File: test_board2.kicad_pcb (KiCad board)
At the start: 2 copper layers, 73.7 x 101.6 mm, 67 parts, among them U1 SM220, U2 AS1116

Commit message: After 1st design review
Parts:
- added BT1, BT2: 1.5V, Synapse:BATT_2466, F.Cu at (177.8, 152.3)
- added C1, C18, C2: 100nF, Capacitors_SMD:C_0603, F.Cu at (177.8, 152.3)
- added C10, C12, C14, C8: 0.1uF, Capacitors_SMD:C_0603, F.Cu at (177.8, 152.3)
- added C11, C13, C15, C17, C19, C7, C9: 4.7uF, Capacitors_SMD:C_0603, F.Cu at (177.8, 152.3)
- added C16, C3: 10uF, Capacitors_SMD:C_0603, F.Cu at (177.8, 152.3)
- added C4: 10nF, Capacitors_SMD:C_0603, F.Cu at (177.8, 152.3)
- added C5, C6: 47pF, Capacitors_SMD:C_0603, F.Cu at (177.8, 152.3)
- added D65: LED, w_smd_leds:Led_0603, F.Cu at (172.2, 150.7)
- added D66, D67, D68: LED, w_smd_leds:Led_0603, F.Cu at (177.8, 152.3)
- added D69, D70, D71, D72, D73, D74, D75: 1N4148W, Diodes_SMD:SOD-123, F.Cu at (177.8, 152.3)
- added FB1: 600 OHM 500MA, Resistors_SMD:R_0603, F.Cu at (177.8, 152.3)
- added L1: 4.7uH 0.9A, Synapse:TYS-2, F.Cu at (177.8, 152.3)
- added P1: USB_B, w_conn_pc:conn_usb_B_micro_smd-2, F.Cu at (152.7, 152.7)
- added P2, P3: CONN_01X08, Pin_Headers:Pin_Header_Straight_1x08, F.Cu at (177.8, 152.3)
- added P4: CONN_01X10, Pin_Headers:Pin_Header_Straight_1x10, F.Cu at (177.8, 152.3)
- added P5: CONN_01X06, Pin_Headers:Pin_Header_Straight_1x06, F.Cu at (177.8, 152.3)
- added P6: CONN_02X03, Pin_Headers:Pin_Header_Straight_2x03, F.Cu at (177.8, 152.3)
- added Q1: ZXMN2F30FHCT-ND, TO_SOT_Packages_SMD:SOT-23, F.Cu at (164.7, 149.9)
- added R10: 100k, Resistors_SMD:R_0603, F.Cu at (177.8, 152.3)
- added R11: 1M, Resistors_SMD:R_0603, F.Cu at (177.8, 152.3)
- added R2, R3: 27, Resistors_SMD:R_0603, F.Cu at (177.8, 152.3)
- added R4, R5, R6: 270, Resistors_SMD:R_0603, F.Cu at (177.8, 152.3)
- added R7, R8: 1k, Resistors_SMD:R_0603, F.Cu at (177.8, 152.3)
- added R9: 200k, Resistors_SMD:R_0603, F.Cu at (177.8, 152.3)
- added SW1: SWITCH_DPDT, Synapse:SO-DPDT-6, F.Cu at (177.8, 152.3)
- added SW2, SW3, SW4: SW_PUSH, Buttons_Switches_SMD:SW_SPST_PTS645, F.Cu at (177.8, 152.3)
- added SW5: SW_DIP_8, Synapse:DIPSW-16, F.Cu at (177.8, 152.3)
- added U3: FT230XS, Housings_SSOP:SSOP-16_3.9x4.9mm_Pitch0.635mm, F.Cu at (138.3, 151.5)
- added U4: LD1117S33CTR, TO_SOT_Packages_SMD:SOT-223, F.Cu at (198.4, 152.1)
- added U5: LIS3DH, Synapse:LGA16_3x3, F.Cu at (177.8, 152.3)
- added U6: TPS61070, TO_SOT_Packages_SMD:TSOT-6-MK06A, F.Cu at (177.8, 152.3)
- D2: value LED -> 1N4148W
- U2: value AS1116 -> AS1115
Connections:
- D1 pad 1: Net-(D1-Pad1) -> /STATUS_LED
- D1 pad 2: /SEGA -> Net-(D1-Pad2)
- D10 pad 1: Net-(D10-Pad1) -> /LED_matrix/DIG7
- D10 pad 2: /SEGB -> /LED_matrix/SEGA
- D11 pad 1: Net-(D11-Pad1) -> /LED_matrix/DIG0
- D11 pad 2: /SEGB -> /LED_matrix/SEGB
- D12 pad 1: Net-(D12-Pad1) -> /LED_matrix/DIG1
- D12 pad 2: /SEGB -> /LED_matrix/SEGB
- D13 pad 1: Net-(D13-Pad1) -> /LED_matrix/DIG2
- D13 pad 2: /SEGB -> /LED_matrix/SEGB
- D14 pad 1: Net-(D14-Pad1) -> /LED_matrix/DIG3
- D14 pad 2: /SEGB -> /LED_matrix/SEGB
- D15 pad 1: Net-(D15-Pad1) -> /LED_matrix/DIG4
- D15 pad 2: /SEGB -> /LED_matrix/SEGB
- D16 pad 1: Net-(D16-Pad1) -> /LED_matrix/DIG5
- D16 pad 2: /SEGB -> /LED_matrix/SEGB
- D17 pad 1: Net-(D1-Pad1) -> /LED_matrix/DIG6
- D17 pad 2: /SEGC -> /LED_matrix/SEGB
- D18 pad 1: Net-(D10-Pad1) -> /LED_matrix/DIG7
- D18 pad 2: /SEGC -> /LED_matrix/SEGB
- D19 pad 1: Net-(D11-Pad1) -> /LED_matrix/DIG0
- D19 pad 2: /SEGC -> /LED_matrix/SEGC
- D2 pad 1: Net-(D10-Pad1) -> Net-(D2-Pad1)
- D2 pad 2: /SEGA -> /LED_matrix/SEGA
- D20 pad 1: Net-(D12-Pad1) -> /LED_matrix/DIG1
- D20 pad 2: /SEGC -> /LED_matrix/SEGC
- D21 pad 1: Net-(D13-Pad1) -> /LED_matrix/DIG2
- D21 pad 2: /SEGC -> /LED_matrix/SEGC
- D22 pad 1: Net-(D14-Pad1) -> /LED_matrix/DIG3
- D22 pad 2: /SEGC -> /LED_matrix/SEGC
- D23 pad 1: Net-(D15-Pad1) -> /LED_matrix/DIG4
- D23 pad 2: /SEGC -> /LED_matrix/SEGC
- D24 pad 1: Net-(D16-Pad1) -> /LED_matrix/DIG5
- D24 pad 2: /SEGC -> /LED_matrix/SEGC
- D25 pad 1: Net-(D1-Pad1) -> /LED_matrix/DIG6
- D25 pad 2: /SEGD -> /LED_matrix/SEGC
- D26 pad 1: Net-(D10-Pad1) -> /LED_matrix/DIG7
- D26 pad 2: /SEGD -> /LED_matrix/SEGC
- D27 pad 1: Net-(D11-Pad1) -> /LED_matrix/DIG0
- D27 pad 2: /SEGD -> /LED_matrix/SEGD
- D28 pad 1: Net-(D12-Pad1) -> /LED_matrix/DIG1
- D28 pad 2: /SEGD -> /LED_matrix/SEGD
- D29 pad 1: Net-(D13-Pad1) -> /LED_matrix/DIG2
- D29 pad 2: /SEGD -> /LED_matrix/SEGD
- D3 pad 1: Net-(D11-Pad1) -> /LED_matrix/DIG0
- D3 pad 2: /SEGA -> /LED_matrix/SEGA
- D30 pad 1: Net-(D14-Pad1) -> /LED_matrix/DIG3
- D30 pad 2: /SEGD -> /LED_matrix/SEGD
- D31 pad 1: Net-(D15-Pad1) -> /LED_matrix/DIG4
- D31 pad 2: /SEGD -> /LED_matrix/SEGD
- D32 pad 1: Net-(D16-Pad1) -> /LED_matrix/DIG5
- D32 pad 2: /SEGD -> /LED_matrix/SEGD
- D33 pad 1: Net-(D1-Pad1) -> /LED_matrix/DIG6
- D33 pad 2: /SEGE -> /LED_matrix/SEGD
- D34 pad 1: Net-(D10-Pad1) -> /LED_matrix/DIG7
- D34 pad 2: /SEGE -> /LED_matrix/SEGD
- D35 pad 1: Net-(D11-Pad1) -> /LED_matrix/DIG0
- D35 pad 2: /SEGE -> /LED_matrix/SEGE
- D36 pad 1: Net-(D12-Pad1) -> /LED_matrix/DIG1
- D36 pad 2: /SEGE -> /LED_matrix/SEGE
- D37 pad 1: Net-(D13-Pad1) -> /LED_matrix/DIG2
- D37 pad 2: /SEGE -> /LED_matrix/SEGE
- D38 pad 1: Net-(D14-Pad1) -> /LED_matrix/DIG3
- D38 pad 2: /SEGE -> /LED_matrix/SEGE
- D39 pad 1: Net-(D15-Pad1) -> /LED_matrix/DIG4
- D39 pad 2: /SEGE -> /LED_matrix/SEGE
- D4 pad 1: Net-(D12-Pad1) -> /LED_matrix/DIG1
- D4 pad 2: /SEGA -> /LED_matrix/SEGA
- D40 pad 1: Net-(D16-Pad1) -> /LED_matrix/DIG5
- D40 pad 2: /SEGE -> /LED_matrix/SEGE
- D41 pad 1: Net-(D1-Pad1) -> /LED_matrix/DIG6
- D41 pad 2: /SEGF -> /LED_matrix/SEGE
- D42 pad 1: Net-(D10-Pad1) -> /LED_matrix/DIG7
- D42 pad 2: /SEGF -> /LED_matrix/SEGE
- D43 pad 1: Net-(D11-Pad1) -> /LED_matrix/DIG0
- D43 pad 2: /SEGF -> /LED_matrix/SEGF
- D44 pad 1: Net-(D12-Pad1) -> /LED_matrix/DIG1
- D44 pad 2: /SEGF -> /LED_matrix/SEGF
- D45 pad 1: Net-(D13-Pad1) -> /LED_matrix/DIG2
- D45 pad 2: /SEGF -> /LED_matrix/SEGF
- D46 pad 1: Net-(D14-Pad1) -> /LED_matrix/DIG3
- D46 pad 2: /SEGF -> /LED_matrix/SEGF
- D47 pad 1: Net-(D15-Pad1) -> /LED_matrix/DIG4
- D47 pad 2: /SEGF -> /LED_matrix/SEGF
- D48 pad 1: Net-(D16-Pad1) -> /LED_matrix/DIG5
- D48 pad 2: /SEGF -> /LED_matrix/SEGF
- D49 pad 1: Net-(D1-Pad1) -> /LED_matrix/DIG6
- D49 pad 2: /SEGG -> /LED_matrix/SEGF
- D5 pad 1: Net-(D13-Pad1) -> /LED_matrix/DIG2
- D5 pad 2: /SEGA -> /LED_matrix/SEGA
- D50 pad 1: Net-(D10-Pad1) -> /LED_matrix/DIG7
- D50 pad 2: /SEGG -> /LED_matrix/SEGF
- D51 pad 1: Net-(D11-Pad1) -> /LED_matrix/DIG0
- D51 pad 2: /SEGG -> /LED_matrix/SEGG
- D52 pad 1: Net-(D12-Pad1) -> /LED_matrix/DIG1
- D52 pad 2: /SEGG -> /LED_matrix/SEGG
- D53 pad 1: Net-(D13-Pad1) -> /LED_matrix/DIG2
- D53 pad 2: /SEGG -> /LED_matrix/SEGG
- D54 pad 1: Net-(D14-Pad1) -> /LED_matrix/DIG3
- D54 pad 2: /SEGG -> /LED_matrix/SEGG
- D55 pad 1: Net-(D15-Pad1) -> /LED_matrix/DIG4
- D55 pad 2: /SEGG -> /LED_matrix/SEGG
- D56 pad 1: Net-(D16-Pad1) -> /LED_matrix/DIG5
- D56 pad 2: /SEGG -> /LED_matrix/SEGG
- D57 pad 1: Net-(D1-Pad1) -> /LED_matrix/DIG6
- D57 pad 2: /SEGDP -> /LED_matrix/SEGG
- D58 pad 1: Net-(D10-Pad1) -> /LED_matrix/DIG7
- D58 pad 2: /SEGDP -> /LED_matrix/SEGG
- D59 pad 1: Net-(D11-Pad1) -> /LED_matrix/DIG0
- D59 pad 2: /SEGDP -> /LED_matrix/SEGDP
- D6 pad 1: Net-(D14-Pad1) -> /LED_matrix/DIG3
- D6 pad 2: /SEGA -> /LED_matrix/SEGA
- D60 pad 1: Net-(D12-Pad1) -> /LED_matrix/DIG1
- D60 pad 2: /SEGDP -> /LED_matrix/SEGDP
- D61 pad 1: Net-(D13-Pad1) -> /LED_matrix/DIG2
- D61 pad 2: /SEGDP -> /LED_matrix/SEGDP
- D62 pad 1: Net-(D14-Pad1) -> /LED_matrix/DIG3
- D62 pad 2: /SEGDP -> /LED_matrix/SEGDP
- D63 pad 1: Net-(D15-Pad1) -> /LED_matrix/DIG4
- D63 pad 2: /SEGDP -> /LED_matrix/SEGDP
- D64 pad 1: Net-(D16-Pad1) -> /LED_matrix/DIG5
- D64 pad 2: /SEGDP -> /LED_matrix/SEGDP
- D7 pad 1: Net-(D15-Pad1) -> /LED_matrix/DIG4
- D7 pad 2: /SEGA -> /LED_matrix/SEGA
- D8 pad 1: Net-(D16-Pad1) -> /LED_matrix/DIG5
- D8 pad 2: /SEGA -> /LED_matrix/SEGA
- D9 pad 1: Net-(D1-Pad1) -> /LED_matrix/DIG6
- D9 pad 2: /SEGB -> /LED_matrix/SEGA
- R1 pad 1: VCC -> /LED_matrix/LED_3V
- U1 pad A4: Net-(U1-PadA4) -> /PF0
- U1 pad A5: /SCLK -> Net-(U1-PadA5)
- U1 pad A6: Net-(U1-PadA6) -> /PF4
- U1 pad A7: Net-(U1-PadA7) -> /PF6
- U1 pad B1: /MISO -> Net-(U1-PadB1)
- U1 pad B2: /LED_LD -> /PE3
- U1 pad B3: Net-(U1-PadB3) -> /PE5
- U1 pad B4: /MOSI -> /PF1
- U1 pad B6: Net-(U1-PadB6) -> /PF5
- U1 pad B7: Net-(U1-PadB7) -> /PF7
- U1 pad C1: Net-(U1-PadC1) -> /PE0
- U1 pad C2: Net-(U1-PadC2) -> /PE1
- U1 pad C3: Net-(U1-PadC3) -> /PE4
- U1 pad C4: Net-(U1-PadC4) -> /BTN_RT
- U1 pad C5: Net-(U1-PadC5) -> /PE7
- U1 pad D1: Net-(U1-PadD1) -> /PB5
- U1 pad D2: Net-(U1-PadD2) -> /PB6
- U1 pad D3: Net-(U1-PadD3) -> /PB7
- U1 pad E1: Net-(U1-PadE1) -> /MOSI
- U1 pad E2: Net-(U1-PadE2) -> /MISO
- U1 pad E3: Net-(U1-PadE3) -> /ACC_INT1
- U1 pad F1: Net-(U1-PadF1) -> /BTN_LFT
- U1 pad F2: Net-(U1-PadF2) -> /SCLK
- U1 pad F3: Net-(U1-PadF3) -> I2C_SDA
- U1 pad F4: Net-(U1-PadF4) -> I2C_SCL
- U1 pad G2: Net-(U1-PadG2) -> /*IS_USB
- U1 pad G3: Net-(U1-PadG3) -> /PD4
- U1 pad G4: Net-(U1-PadG4) -> /USB_TXD
- U1 pad G5: Net-(U1-PadG5) -> /STATUS_LED
- U1 pad H2: Net-(U1-PadH2) -> /ACC_INT2
- U1 pad H3: Net-(U1-PadH3) -> LED_PWR_EN
- U1 pad H4: Net-(U1-PadH4) -> /USB_RXD
- U1 pad H5: Net-(U1-PadH5) -> /*RESET
- U2 pad 1: /MOSI -> I2C_SDA
- U2 pad 10: /DIG7 -> /LED_matrix/DIG7
- U2 pad 11: /LED_LD -> Net-(U2-Pad11)
- U2 pad 14: /SCLK -> I2C_SCL
- U2 pad 15: /SEGA -> /LED_matrix/SEGA
- U2 pad 16: /SEGF -> /LED_matrix/SEGF
- U2 pad 17: /SEGB -> /LED_matrix/SEGB
- U2 pad 18: /SEGG -> /LED_matrix/SEGG
- U2 pad 19: VCC -> /LED_matrix/LED_3V
- U2 pad 2: /DIG0 -> /LED_matrix/DIG0
- U2 pad 20: /SEGC -> /LED_matrix/SEGC
- U2 pad 21: /SEGE -> /LED_matrix/SEGE
- U2 pad 22: /SEGDP -> /LED_matrix/SEGDP
- U2 pad 23: /SEGD -> /LED_matrix/SEGD
- U2 pad 24: /MISO -> Net-(U2-Pad24)
- U2 pad 3: /DIG1 -> /LED_matrix/DIG1
- U2 pad 4: /DIG2 -> /LED_matrix/DIG2
- U2 pad 5: /DIG3 -> /LED_matrix/DIG3
- U2 pad 7: /DIG4 -> /LED_matrix/DIG4
- U2 pad 8: /DIG5 -> /LED_matrix/DIG5
- U2 pad 9: /DIG6 -> /LED_matrix/DIG6

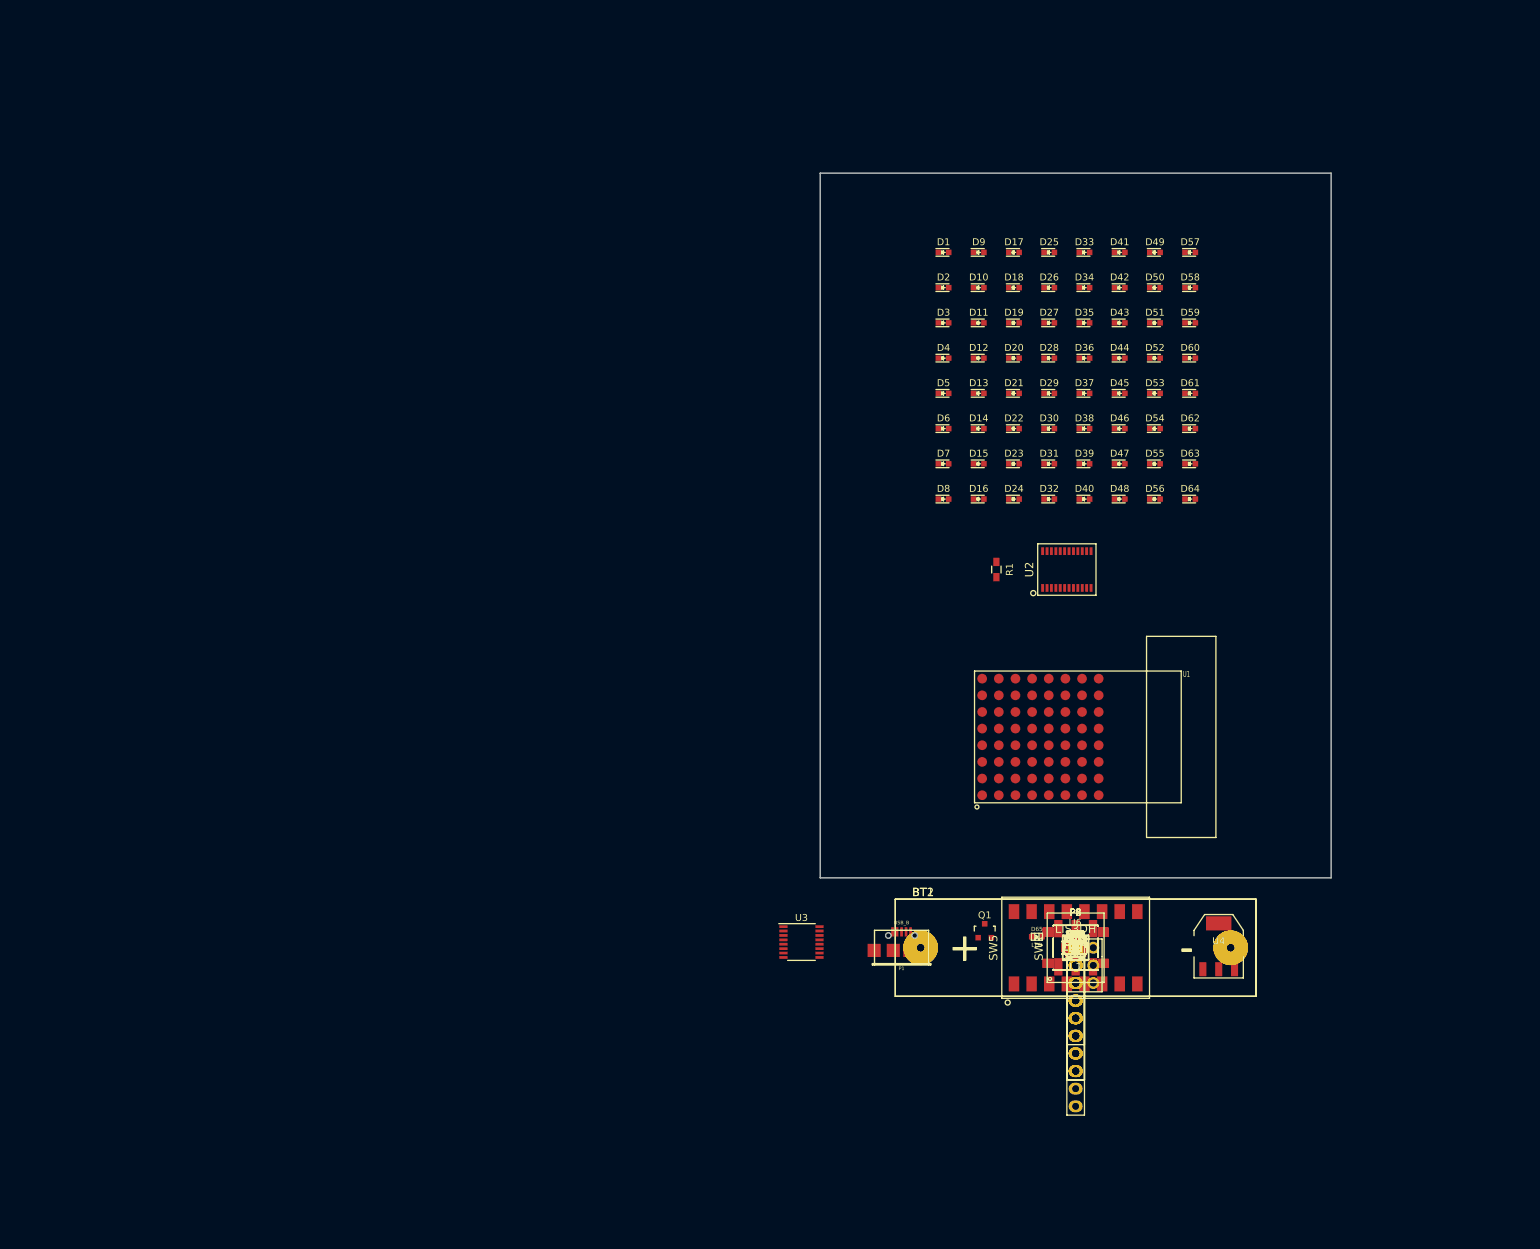
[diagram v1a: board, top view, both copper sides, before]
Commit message: Arduino footprint laid out
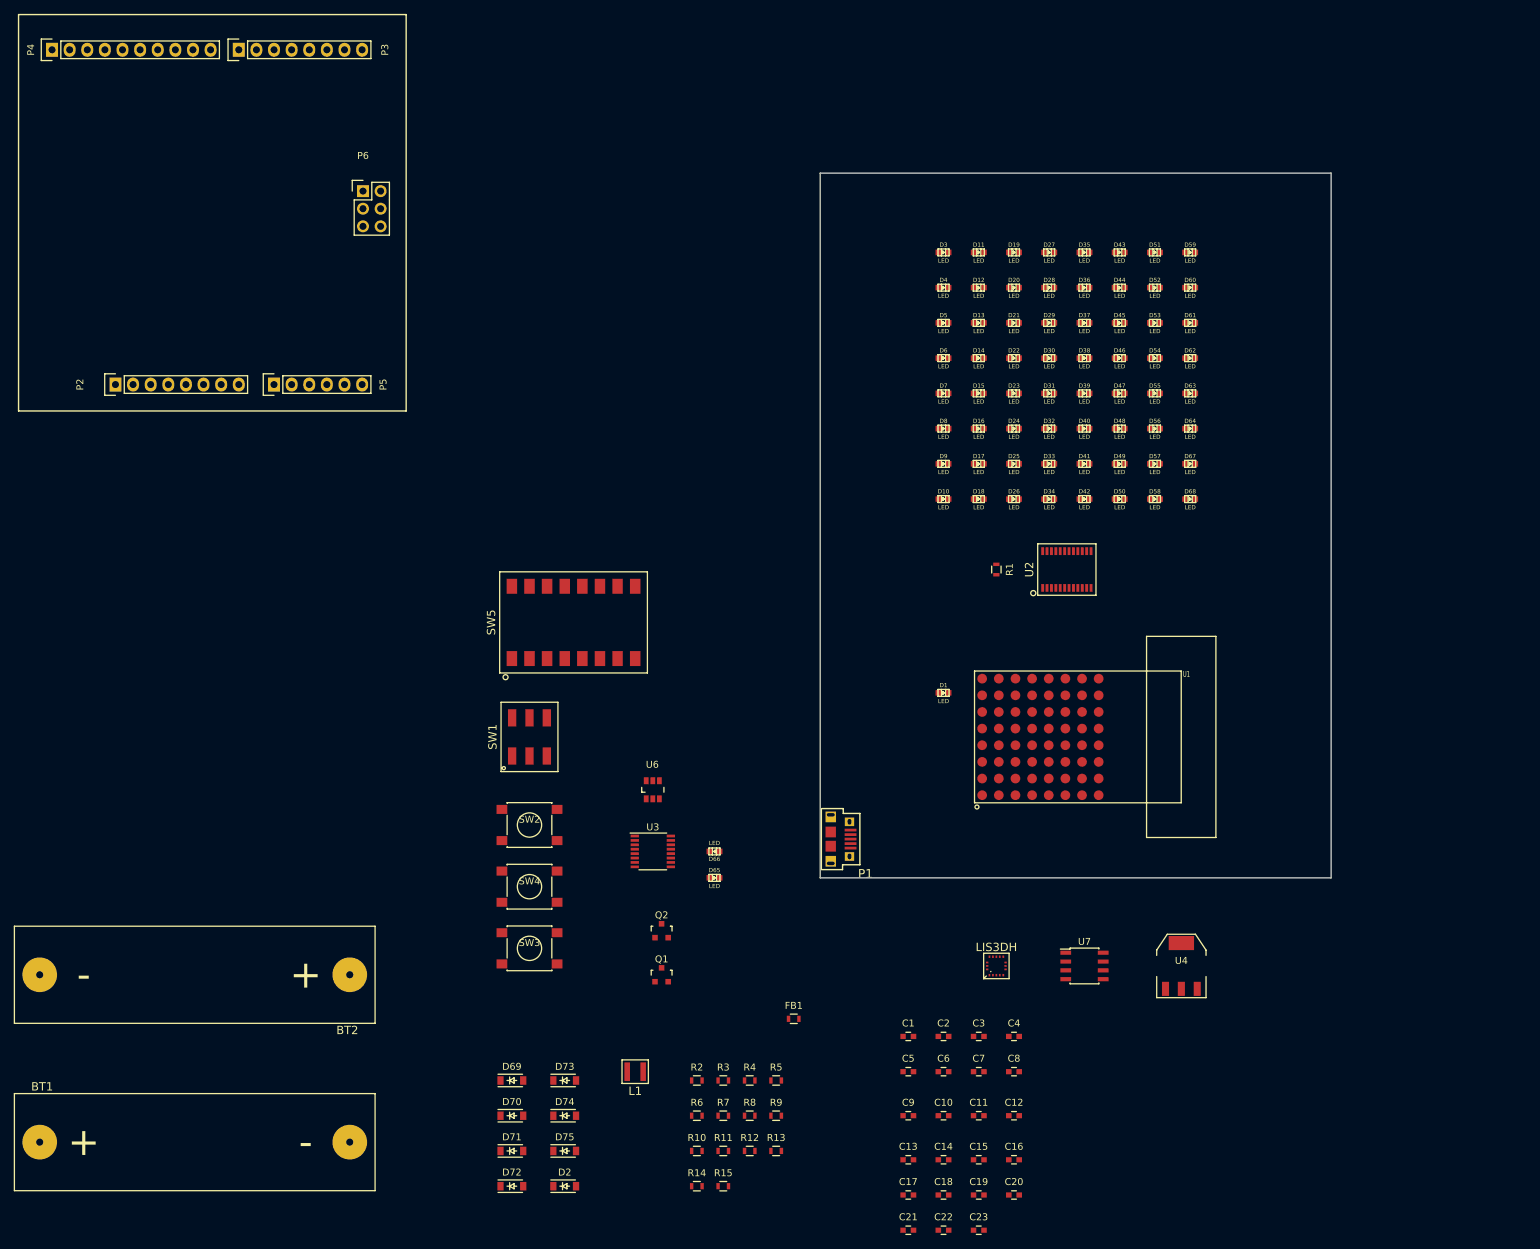
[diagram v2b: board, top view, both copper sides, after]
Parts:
- added C20: 0.1uF, Capacitors_SMD:C_0603, F.Cu at (168.9, 188.0)
- added C21: 100nF, Capacitors_SMD:C_0603, F.Cu at (153.7, 193.0)
- added C22: 22uF, Capacitors_SMD:C_0603, F.Cu at (158.8, 193.0)
- added C23: 22uF, Capacitors_SMD:C_0603, F.Cu at (163.8, 193.0)
- added Q2: Si2305DS, TO_SOT_Packages_SMD:SOT-23, F.Cu at (118.1, 149.9)
- added R12: 100k, Resistors_SMD:R_0603, F.Cu at (130.8, 181.6)
- added R13: 39k, Resistors_SMD:R_0603, F.Cu at (134.6, 181.6)
- added R14: 4.7k, Resistors_SMD:R_0603, F.Cu at (123.2, 186.7)
- added R15: 4.7k, Resistors_SMD:R_0603, F.Cu at (127.0, 186.7)
- added U7: NLSX4373, Housings_SOIC:SOIC-8_3.9x4.9mm_Pitch1.27mm, F.Cu at (179.1, 154.9)
- C7: value 4.7uF -> 22uF
- C8: value 0.1uF -> 22uF
- D1, D10, D11, D12, D13, D14, D15, D16, D17, D18, D19, D20, D21, D22, D23, D24, D25, D26, D27, D28, D29, D3, D30, D31, D32, D33, D34, D35, D36, D37, D38, D39, D4, D40, D41, D42, D43, D44, D45, D46, D47, D48, D49, D5, D50, D51, D52, D53, D54, D55, D56, D57, D58, D59, D6, D60, D61, D62, D63, D64, D7, D8, D9: footprint LEDs:LED-0603 -> w_smd_leds:Led_0603
- D2: footprint LEDs:LED-0603 -> Diodes_SMD:SOD-123
- P1: value USB_B -> MicroB; footprint w_conn_pc:conn_usb_B_micro_smd-2 -> Synapse:USBmicroB
- R1: value 12k -> 10k; footprint Resistors_SMD:R_0603_HandSoldering -> Resistors_SMD:R_0603
- moved P4 196.3 mm to (30.2, 22.9), turned to 90 degrees
- moved P3 177.0 mm to (57.1, 22.9), turned to 90 degrees
- moved P2 160.5 mm to (39.4, 71.1), turned to 90 degrees
- moved P6 149.9 mm to (75.1, 43.2)
- moved P5 141.2 mm to (62.2, 71.1), turned to 90 degrees
- moved D2 140.6 mm to (104.1, 186.7)
- moved BT1 130.1 mm to (50.8, 180.3)
- moved BT2 127.1 mm to (50.8, 156.2), turned to 180 degrees
- moved D72 88.3 mm to (96.5, 186.7)
- moved D71 86.4 mm to (96.5, 181.6)
- moved SW5 86.3 mm to (105.4, 105.4)
- moved D70 84.8 mm to (96.5, 176.5)
- moved SW1 84.4 mm to (99.1, 121.9)
- moved D69 83.5 mm to (96.5, 171.4)
- moved SW2 80.7 mm to (99.1, 134.6)
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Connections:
- C13 pad 1: VCC -> /LED_matrix/LED_3V
- C14 pad 1: VCC -> /LED_matrix/LED_3V
- C8 pad 1: VCC -> Net-(BT2-Pad1)
- D10 pad 2: /LED_matrix/SEGA -> /LED_matrix/SEGDP
- D11 pad 2: /LED_matrix/SEGB -> /LED_matrix/SEGA
- D12 pad 2: /LED_matrix/SEGB -> /LED_matrix/SEGA
- D13 pad 2: /LED_matrix/SEGB -> /LED_matrix/SEGA
- D14 pad 2: /LED_matrix/SEGB -> /LED_matrix/SEGA
- D15 pad 2: /LED_matrix/SEGB -> /LED_matrix/SEGA
- D16 pad 2: /LED_matrix/SEGB -> /LED_matrix/SEGA
- D17 pad 2: /LED_matrix/SEGB -> /LED_matrix/SEGA
- D18 pad 2: /LED_matrix/SEGB -> /LED_matrix/SEGA
- D19 pad 2: /LED_matrix/SEGC -> /LED_matrix/SEGB
- D2 pad 2: /LED_matrix/SEGA -> /LED_matrix/SEGDP
- D20 pad 2: /LED_matrix/SEGC -> /LED_matrix/SEGB
- D21 pad 2: /LED_matrix/SEGC -> /LED_matrix/SEGB
- D22 pad 2: /LED_matrix/SEGC -> /LED_matrix/SEGB
- D23 pad 2: /LED_matrix/SEGC -> /LED_matrix/SEGB
- D24 pad 2: /LED_matrix/SEGC -> /LED_matrix/SEGB
- D25 pad 2: /LED_matrix/SEGC -> /LED_matrix/SEGB
- D26 pad 2: /LED_matrix/SEGC -> /LED_matrix/SEGB
- D27 pad 2: /LED_matrix/SEGD -> /LED_matrix/SEGC
- D28 pad 2: /LED_matrix/SEGD -> /LED_matrix/SEGC
- D29 pad 2: /LED_matrix/SEGD -> /LED_matrix/SEGC
- D3 pad 2: /LED_matrix/SEGA -> /LED_matrix/SEGDP
- D30 pad 2: /LED_matrix/SEGD -> /LED_matrix/SEGC
- D31 pad 2: /LED_matrix/SEGD -> /LED_matrix/SEGC
- D32 pad 2: /LED_matrix/SEGD -> /LED_matrix/SEGC
- D33 pad 2: /LED_matrix/SEGD -> /LED_matrix/SEGC
- D34 pad 2: /LED_matrix/SEGD -> /LED_matrix/SEGC
- D35 pad 2: /LED_matrix/SEGE -> /LED_matrix/SEGD
- D36 pad 2: /LED_matrix/SEGE -> /LED_matrix/SEGD
- D37 pad 2: /LED_matrix/SEGE -> /LED_matrix/SEGD
- D38 pad 2: /LED_matrix/SEGE -> /LED_matrix/SEGD
- D39 pad 2: /LED_matrix/SEGE -> /LED_matrix/SEGD
- D4 pad 2: /LED_matrix/SEGA -> /LED_matrix/SEGDP
- D40 pad 2: /LED_matrix/SEGE -> /LED_matrix/SEGD
- D41 pad 2: /LED_matrix/SEGE -> /LED_matrix/SEGD
- D42 pad 2: /LED_matrix/SEGE -> /LED_matrix/SEGD
- D43 pad 2: /LED_matrix/SEGF -> /LED_matrix/SEGE
- D44 pad 2: /LED_matrix/SEGF -> /LED_matrix/SEGE
- D45 pad 2: /LED_matrix/SEGF -> /LED_matrix/SEGE
- D46 pad 2: /LED_matrix/SEGF -> /LED_matrix/SEGE
- D47 pad 2: /LED_matrix/SEGF -> /LED_matrix/SEGE
- D48 pad 2: /LED_matrix/SEGF -> /LED_matrix/SEGE
- D49 pad 2: /LED_matrix/SEGF -> /LED_matrix/SEGE
- D5 pad 2: /LED_matrix/SEGA -> /LED_matrix/SEGDP
- D50 pad 2: /LED_matrix/SEGF -> /LED_matrix/SEGE
- D51 pad 2: /LED_matrix/SEGG -> /LED_matrix/SEGF
- D52 pad 2: /LED_matrix/SEGG -> /LED_matrix/SEGF
- D53 pad 2: /LED_matrix/SEGG -> /LED_matrix/SEGF
- D54 pad 2: /LED_matrix/SEGG -> /LED_matrix/SEGF
- D55 pad 2: /LED_matrix/SEGG -> /LED_matrix/SEGF
- D56 pad 2: /LED_matrix/SEGG -> /LED_matrix/SEGF
- D57 pad 2: /LED_matrix/SEGG -> /LED_matrix/SEGF
- D58 pad 2: /LED_matrix/SEGG -> /LED_matrix/SEGF
- D59 pad 2: /LED_matrix/SEGDP -> /LED_matrix/SEGG
- D6 pad 2: /LED_matrix/SEGA -> /LED_matrix/SEGDP
- D60 pad 2: /LED_matrix/SEGDP -> /LED_matrix/SEGG
- D61 pad 2: /LED_matrix/SEGDP -> /LED_matrix/SEGG
- D62 pad 2: /LED_matrix/SEGDP -> /LED_matrix/SEGG
- D63 pad 2: /LED_matrix/SEGDP -> /LED_matrix/SEGG
- D64 pad 2: /LED_matrix/SEGDP -> /LED_matrix/SEGG
- D67 pad 2: /LED_matrix/SEGDP -> /LED_matrix/SEGG
- D68 pad 2: /LED_matrix/SEGDP -> /LED_matrix/SEGG
- D69 pad 2: /LED_matrix/SEGB -> /LED_matrix/SEGA
- D7 pad 2: /LED_matrix/SEGA -> /LED_matrix/SEGDP
- D70 pad 2: /LED_matrix/SEGC -> /LED_matrix/SEGB
- D71 pad 2: /LED_matrix/SEGD -> /LED_matrix/SEGC
- D72 pad 2: /LED_matrix/SEGE -> /LED_matrix/SEGD
- D73 pad 2: /LED_matrix/SEGF -> /LED_matrix/SEGE
- D74 pad 2: /LED_matrix/SEGG -> /LED_matrix/SEGF
- D75 pad 2: /LED_matrix/SEGDP -> /LED_matrix/SEGG
- D8 pad 2: /LED_matrix/SEGA -> /LED_matrix/SEGDP
- D9 pad 2: /LED_matrix/SEGA -> /LED_matrix/SEGDP
- FB1 pad 2: /VREG_IN -> /VIN_USB
- Q1 pad 1: Net-(BT1-Pad2) -> Net-(Q1-Pad1)
- Q1 pad 2: Net-(BT2-Pad1) -> GND
- Q1 pad 3: GND -> Net-(BT1-Pad2)
- U2 pad 1: I2C_SDA -> /LED_matrix/LED_SDA
- U2 pad 14: I2C_SCL -> /LED_matrix/LED_SCL
- U3 pad 12: /VREG_IN -> /VIN_USB

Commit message: First placement
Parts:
- added ?: LanyardSlot, Synapse:LanyardSlot, F.Cu at (175.3, 27.2)
- added REF**: LanyardSlot, Synapse:LanyardSlot, F.Cu at (175.3, 143.5)
- BT1, BT2: moved to B.Cu
- moved P4 182.1 mm to (199.3, 90.6), turned to 0 degrees
- moved P3 170.7 mm to (199.3, 117.5), turned to 0 degrees
- moved BT1 151.3 mm to (189.2, 119.4), turned to 270 degrees
- moved SW3 149.1 mm to (201.9, 44.5), turned to 90 degrees
- moved P6 138.8 mm to (178.9, 135.4), turned to 270 degrees
- moved BT2 116.5 mm to (161.3, 119.4), turned to 90 degrees
- moved P2 115.2 mm to (151.0, 99.7), turned to 0 degrees
- moved SW2 102.9 mm to (148.6, 44.5), turned to 90 degrees
- moved P5 102.6 mm to (151.0, 122.6), turned to 0 degrees
- moved SW1 102.4 mm to (199.4, 142.2), turned to 90 degrees
- moved SW5 83.2 mm to (185.4, 82.5), turned to 270 degrees
- moved SW4 73.0 mm to (161.3, 105.4)
- moved U5 60.3 mm to (226.6, 158.5)
- moved U7 60.3 mm to (239.3, 158.5)
- moved U2 47.6 mm to (149.9, 58.4), turned to 270 degrees
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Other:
- board size 73.7 x 101.6 mm -> 63.5 x 127 mm
- net class Default: clearance 0.2 -> 0.254; trace_width 0.25 -> 0.254; via_dia 0.6 -> 0.762; via_drill 0.4 -> 0.508
- rule trace_clearance: 0.2 -> 0.254
- rule trace_min: 0.2 -> 0.1524
- rule via_min_drill: 0.3 -> 0.254
- rule via_min_size: 0.4 -> 0.4064
- board text added: "ANALOG"
- board text added: "DIGITAL"
- board text added: "HARDWARE"
- board text added: "IoT"
- board text added: "LOGO / TEXT"
- board text added: "S7"
- board text added: "S8"
- board text added: "SOFTWARE"
- board text added: "STEM"

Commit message: Placement v1
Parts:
- D2, D69, D70, D71, D72, D73, D74, D75: footprint Diodes_SMD:SOD-123 -> Diodes_SMD:SOD-323
- P2, P3: footprint Pin_Headers:Pin_Header_Straight_1x08 -> Socket_Strips:Socket_Strip_Straight_1x08
- P4: footprint Pin_Headers:Pin_Header_Straight_1x10 -> Socket_Strips:Socket_Strip_Straight_1x10
- P5: footprint Pin_Headers:Pin_Header_Straight_1x06 -> Socket_Strips:Socket_Strip_Straight_1x06
- moved U6 2.34 mm to (118.4, 131.3)
- moved P1 1.16 mm to (145.5, 141.9)
- moved SW1 0.10 mm to (199.4, 142.3), turned to 180 degrees
- turned P2 to 270 degrees
- turned P3 to 270 degrees
- turned P4 to 270 degrees
- turned P5 to 270 degrees
- renumbered REF** to ?
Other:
- board text added: "BATT"
- board text added: "Collectible"
- board text added: "ESC 2016"
- board text added: "USB"
- board text removed: "LOGO / TEXT"
